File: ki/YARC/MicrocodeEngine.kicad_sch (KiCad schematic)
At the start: 12 parts, among them U32 74HC245, U33 AS6C6264, U34 74LS574, U35 74HC245, U36 AS6C6264, U37 74LS574, U38 74HC245, U39 AS6C6264, U40 74LS574, U41 74HC245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

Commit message: Ongoing fixes for ERC errors
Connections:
- net KI0-1: now also U42.12 (DQ1)
- net KI0-2: now also U42.13 (DQ2)
- net KI0-3: now also U42.15 (DQ3)
- net KI0-4: now also U42.16 (DQ4)
- net KI0-5: now also U42.17 (DQ5)
- net KI0-6: now also U42.18 (DQ6)
- net KI1-10: now also U39.13 (DQ2)
- net KI1-11: now also U39.15 (DQ3)
- net KI1-12: now also U39.16 (DQ4)
- net KI1-13: now also U39.17 (DQ5)
- net KI1-14: now also U39.18 (DQ6)
- net KI2-17: now also U36.12 (DQ1)
- net KI2-18: now also U36.13 (DQ2)
- net KI2-19: now also U36.15 (DQ3)
- net KI2-20: now also U36.16 (DQ4)
- net KI2-21: now also U36.17 (DQ5)
- net KI2-22: now also U36.18 (DQ6)
- net KI3-25: now also U33.12 (DQ1)
- net KI3-26: now also U33.13 (DQ2)
- net KI3-27: now also U33.15 (DQ3)
- net KI3-28: now also U33.16 (DQ4)
- net KI3-29: now also U33.17 (DQ5)
- net KI3-30: now also U33.18 (DQ6)
- net KI1-9: now reaches U39.12 (DQ1)

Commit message: Ongoing schematic changes
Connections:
- net K09 renamed K9
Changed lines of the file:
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@@
     (effects (font (size 1.27 1.27)) (justify left bottom))
   )
-  (label "K09" (at 160.02 26.67 90) (fields_autoplaced)
+  (label "K9" (at 160.02 26.67 90) (fields_autoplaced)
     (effects (font (size 1.27 1.27)) (justify left bottom))
   )

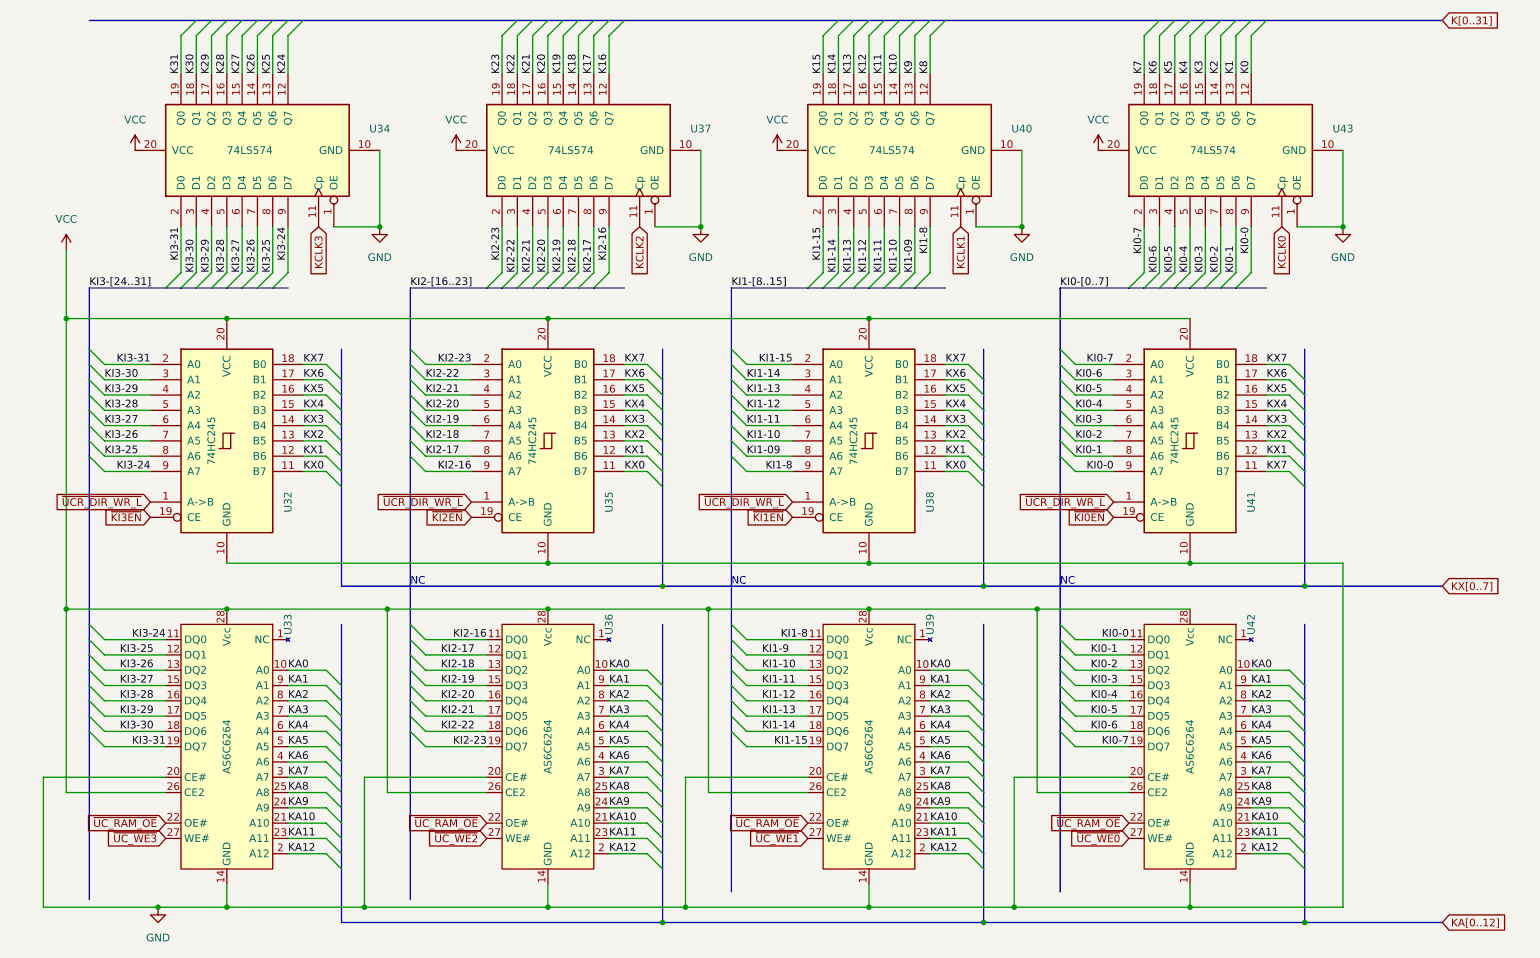
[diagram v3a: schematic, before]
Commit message: Schematic for addressing unit is complete and all ERC violations addressed
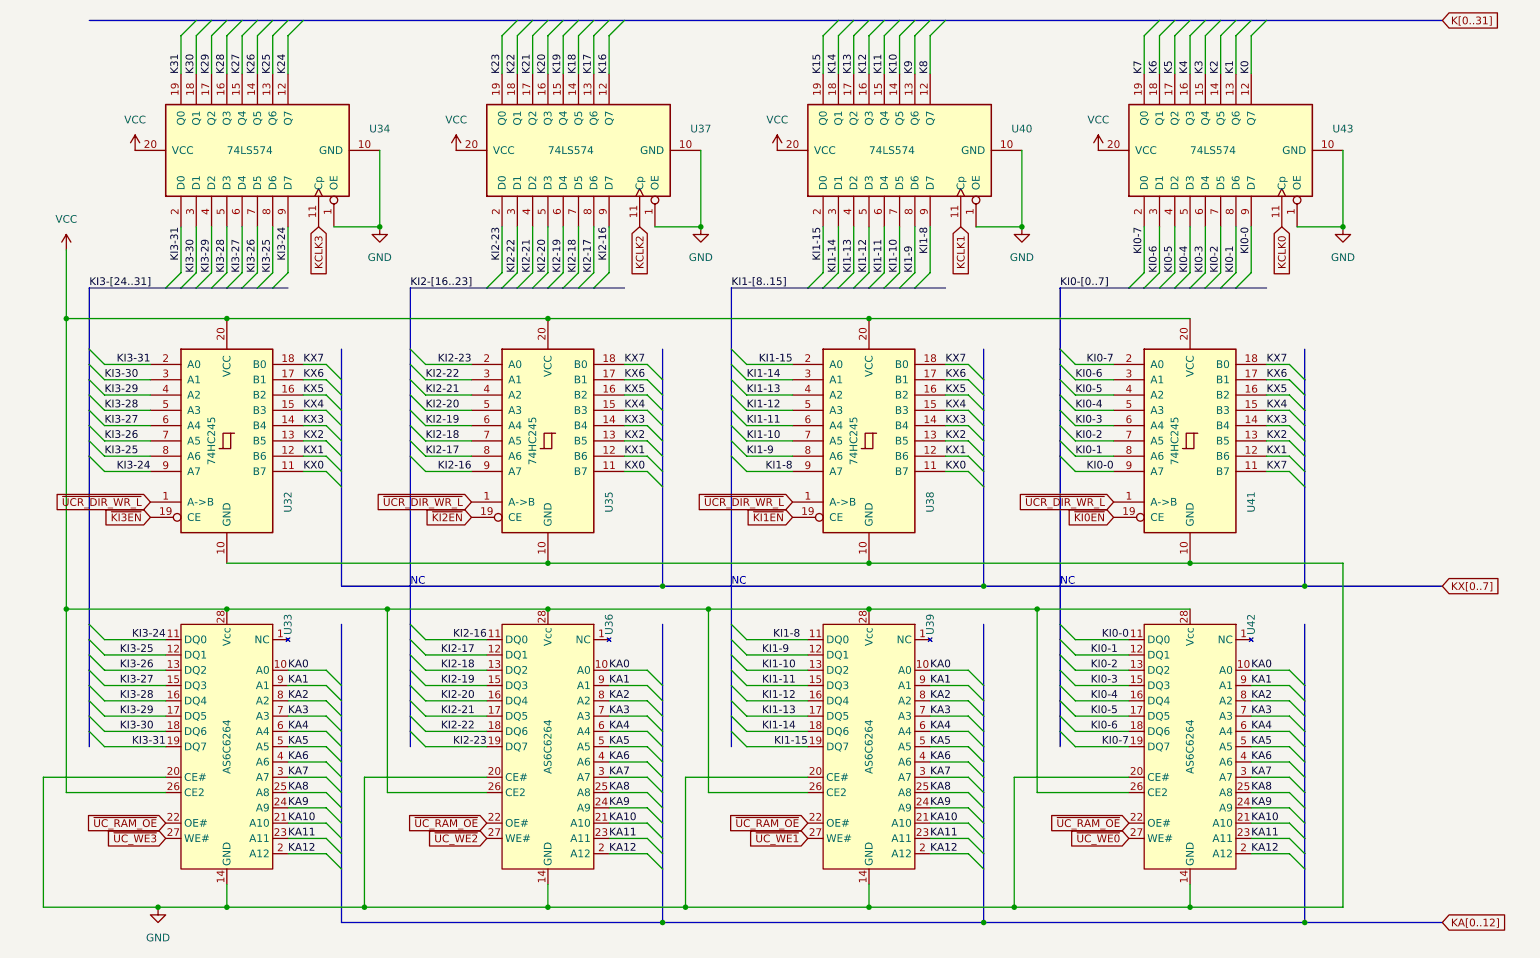
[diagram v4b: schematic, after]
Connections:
- net KI1-09 is gone; now on net KI1-9: U38.8 (A6), U40.8 (D6)
